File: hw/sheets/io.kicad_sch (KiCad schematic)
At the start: 23 parts, among them J2 TYPE-C-31-M-12, J3 TE_292303-7, J4 Hirose_DM3D-SF, J5 Wuerth_694106301002, J6 AudioJack4_Ground, J7 SFW15R-2STE1LF, J8 SFW15R-2STE1LF, J9 TYPE-C-31-M-12, Q1 AO3401A, Q2 AO3401A

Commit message: Add MSC1 breakout (J37), ground J35 spare pads, add audio amp/mic tap (J38)
Carve J35's last 6 pins into a new MSC1 header (J37: CLK/CMD/D0-D3_CD),
keeping J35 at a fixed 26-pin size in both schematic and PCB with the
now-orphaned pads tied to GND. Add a 3-pin tap (J38) off the audio jack
(HPOUTL/GND/MICLP) so an external amplifier or mic can be wired in
directly instead of needing a breakout cable off J6.
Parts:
- added J38: AMP_MIC_TAP, Connector_PinHeader_2.54mm:PinHeader_1x03_P2.54mm_Vertical, symbol Connector_Generic:Conn_01x03
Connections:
- net GND: now also J38.2 (Pin_2)
- net HPOUTL: now also J38.1 (Pin_1)
- net MICLP: now also J38.3 (Pin_3)
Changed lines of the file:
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@@
 		(property "Value" "GND" (at 60.96 241.3 270) (effects (font (size 1.27 1.27))))
+	)
+	(symbol (lib_id "Connector_Generic:Conn_01x03") (at 88.9 241.3 0) (unit 1)
+		(property "Reference" "J38" (at 93.98 238.76000000000002 0) (effects (font (size 1.27 1.27))))
+		(property "Value" "AMP_MIC_TAP" (at 93.98 243.84 0) (effects (font (size 1.27 1.27))))
+		(property "Footprint" "Connector_PinHeader_2.54mm:PinHeader_1x03_P2.54mm_Vertical" (at 88.9 241.3 0) (effects (font (size 1.27 1.27)) hide))
+	)
+	(symbol (lib_id "power:GND") (at 83.82 241.3 270) (unit 1)
+		(property "Reference" "#IGND020" (at 83.82 241.3 0) (effects (font (size 1.27 1.27)) hide))
+		(property "Value" "GND" (at 78.74 241.3 90) (effects (font (size 1.27 1.27))))
 	)
 	(symbol (lib_id "teacup-carrier:SFW15R-2STE1LF_C3167933") (at 190.5 50.8 0) (unit 1)
@@
 	)
 	(symbol (lib_id "power:GND") (at 185.42 45.72 270) (unit 1)
-		(property "Reference" "#IGND020" (at 185.42 45.72 0) (effects (font (size 1.27 1.27)) hide))
+		(property "Reference" "#IGND021" (at 185.42 45.72 0) (effects (font (size 1.27 1.27)) hide))
 		(property "Value" "GND" (at 180.33999999999997 45.72 90) (effects (font (size 1.27 1.27))))
 	)
 	(symbol (lib_id "power:GND") (at 185.42 53.34 270) (unit 1)
-		(property "Reference" "#IGND021" (at 185.42 53.34 0) (effects (font (size 1.27 1.27)) hide))
+		(property "Reference" "#IGND022" (at 185.42 53.34 0) (effects (font (size 1.27 1.27)) hide))
 		(property "Value" "GND" (at 180.33999999999997 53.34 90) (effects (font (size 1.27 1.27))))
 	)
 	(symbol (lib_id "power:GND") (at 185.42 60.96 270) (unit 1)
-		(property "Reference" "#IGND022" (at 185.42 60.96 0) (effects (font (size 1.27 1.27)) hide))
+		(property "Reference" "#IGND023" (at 185.42 60.96 0) (effects (font (size 1.27 1.27)) hide))
 		(property "Value" "GND" (at 180.33999999999997 60.96 90) (effects (font (size 1.27 1.27))))
 	)
 	(symbol (lib_id "power:GND") (at 185.42 68.58 270) (unit 1)
-		(property "Reference" "#IGND023" (at 185.42 68.58 0) (effects (font (size 1.27 1.27)) hide))
+		(property "Reference" "#IGND024" (at 185.42 68.58 0) (effects (font (size 1.27 1.27)) hide))
 		(property "Value" "GND" (at 180.33999999999997 68.58 90) (effects (font (size 1.27 1.27))))
 	)
@@
 	)
 	(symbol (lib_id "power:GND") (at 185.42 121.92 270) (unit 1)
-		(property "Reference" "#IGND024" (at 185.42 121.92 0) (effects (font (size 1.27 1.27)) hide))
+		(property "Reference" "#IGND025" (at 185.42 121.92 0) (effects (font (size 1.27 1.27)) hide))
 		(property "Value" "GND" (at 180.33999999999997 121.92 90) (effects (font (size 1.27 1.27))))
 	)
 	(symbol (lib_id "power:GND") (at 185.42 129.54 270) (unit 1)
-		(property "Reference" "#IGND025" (at 185.42 129.54 0) (effects (font (size 1.27 1.27)) hide))
+		(property "Reference" "#IGND026" (at 185.42 129.54 0) (effects (font (size 1.27 1.27)) hide))
 		(property "Value" "GND" (at 180.33999999999997 129.54 90) (effects (font (size 1.27 1.27))))
 	)
 	(symbol (lib_id "power:GND") (at 185.42 137.16 270) (unit 1)
-		(property "Reference" "#IGND026" (at 185.42 137.16 0) (effects (font (size 1.27 1.27)) hide))
+		(property "Reference" "#IGND027" (at 185.42 137.16 0) (effects (font (size 1.27 1.27)) hide))
 		(property "Value" "GND" (at 180.33999999999997 137.16 90) (effects (font (size 1.27 1.27))))
 	)
 	(symbol (lib_id "power:GND") (at 185.42 144.78 270) (unit 1)
-		(property "Reference" "#IGND027" (at 185.42 144.78 0) (effects (font (size 1.27 1.27)) hide))
+		(property "Reference" "#IGND028" (at 185.42 144.78 0) (effects (font (size 1.27 1.27)) hide))
 		(property "Value" "GND" (at 180.33999999999997 144.78 90) (effects (font (size 1.27 1.27))))
 	)
@@
 	(global_label "HPOUTL" (at 55.88 243.84 0) (effects (font (size 1.27 1.27)) (justify left)))
 	(global_label "MICLP" (at 55.88 238.76 0) (effects (font (size 1.27 1.27)) (justify left)))
+	(global_label "HPOUTL" (at 83.82 238.76 180) (effects (font (size 1.27 1.27)) (justify right)))
+	(global_label "MICLP" (at 83.82 243.84 180) (effects (font (size 1.27 1.27)) (justify right)))
 	(global_label "MIPI0_SCCB_SDA" (at 185.42 35.56 180) (effects (font (size 1.27 1.27)) (justify right)))
 	(global_label "MIPI0_SCCB_SCL" (at 185.42 38.1 180) (effects (font (size 1.27 1.27)) (justify right)))

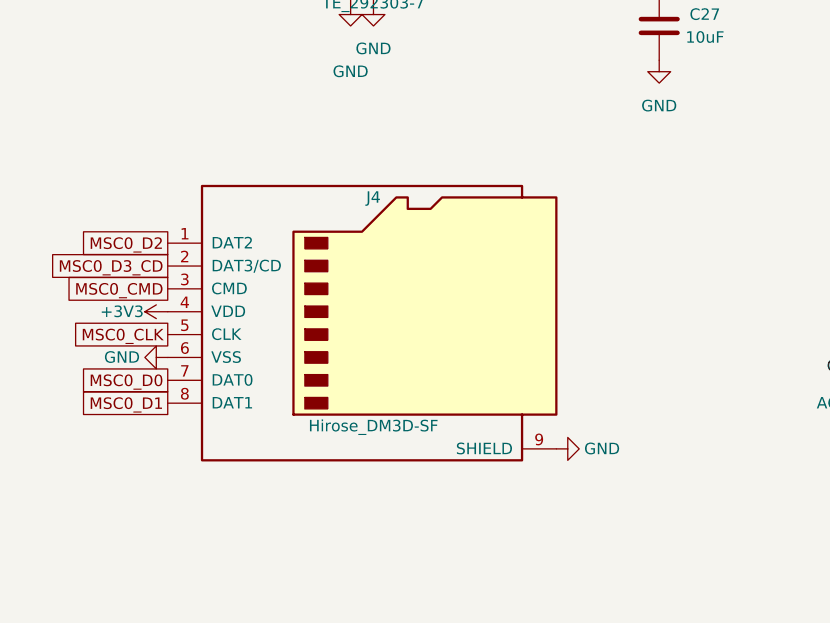
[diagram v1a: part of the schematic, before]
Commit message: Fix schematic<->PCB linking, reorder J1 pins by connected peer, add +3V3 plane, wire microSD card-detect
- schgen.py: deterministic per-symbol UUIDs (uuid5, keyed on ref designator)
  instead of random uuid4, so PCB footprints stay linked to their schematic
  symbol across regenerations; link all 133 real PCB footprints to their
  schematic symbol via path, fixing "Update PCB from Schematic" placing
  duplicates.
- J1 pin reorg: audio (HPOUTL/MICLP) moved from 170/171 to 6/7 (170/171 now
  GND); USBA_HOST_DP/DM moved from 40/41 to 20/21 (40/41 now GND); the 20
  pins connected directly to U8 (ESP32-S3) reordered so U8's ascending pin
  number maps to J1's descending pin number; +5V_MODEA (redundant -- a
  self-contained module already needs its own bare-bench power input)
  replaced with +5V_SW (the real arbitrated switched-5V rail) on pins 17/18.
- New +3V3 copper pour on In1.Cu, mirroring the existing GND pour; every
  +3V3 pad on the board (38, now 39 with R43) gets a stub trace + via down
  to it.
- microSD (J4): switched to the Micro_SD_Card_Det2 symbol so pin 10 (the
  footprint's real card-detect pad) has somewhere to attach; added R43
  (1M, matches TeaCup 3.3's R22) pulling MSC0_CD up to +3V3.
- fp-lib-table: replaced hardcoded /usr/share/kicad/footprints/... paths
  with ${KICAD10_FOOTPRINT_DIR}, fixing "footprint not found" errors for
  every component when Update PCB from Schematic runs outside this Linux
  environment.

Verified throughout via isolated ERC/DRC diffs against pre-change
baselines; each change confirmed to produce only its own intended delta.
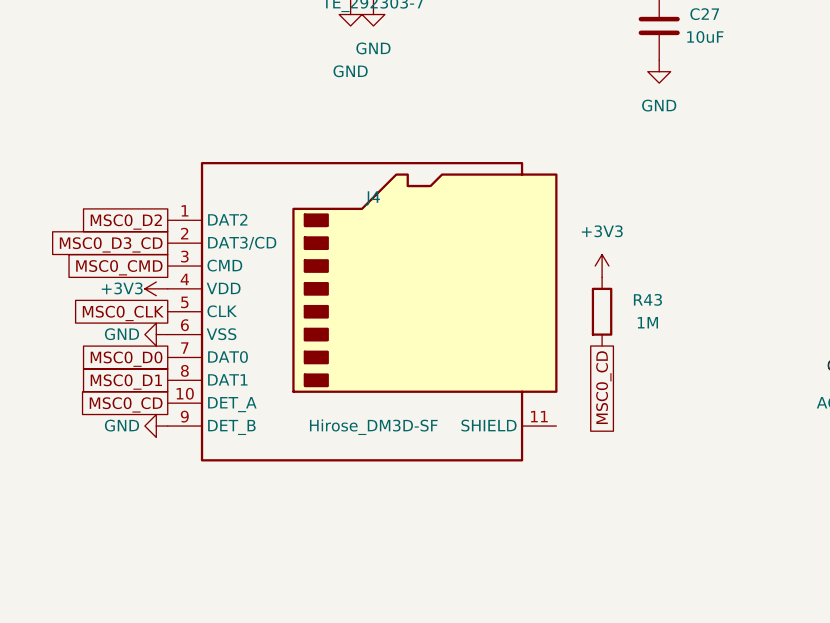
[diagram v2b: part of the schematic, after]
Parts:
- removed J4: Hirose_DM3D-SF, Connector_Card:microSD_HC_Hirose_DM3D-SF, symbol Connector:Micro_SD_Card
- added J4: Hirose_DM3D-SF, Connector_Card:microSD_HC_Hirose_DM3D-SF, symbol Connector:Micro_SD_Card_Det2
- added R43: 1M, Resistor_SMD:R_0402_1005Metric, symbol Device:R
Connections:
- net +3V3: now also J4.4 (VDD), R43.1
- net GND: now also J4.6 (VSS), J4.9 (DET_B)
- net MSC0_CLK: now also J4.5 (CLK)
- net MSC0_CMD: now also J4.3 (CMD)
- net MSC0_D0: now also J4.7 (DAT0)
- net MSC0_D1: now also J4.8 (DAT1)
- net MSC0_D2: now also J4.1 (DAT2)
- net MSC0_D3_CD: now also J4.2 (DAT3/CD)
- new net MSC0_CD: J4.10 (DET_A), R43.2
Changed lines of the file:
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@@
 		(property "Value" "GND" (at 48.26 132.07999999999998 0) (effects (font (size 1.27 1.27))))
 	)
-	(symbol (lib_id "Connector:Micro_SD_Card") (at 50.8 158.75 0) (unit 1)
+	(symbol (lib_id "Connector:Micro_SD_Card_Det2") (at 50.8 158.75 0) (unit 1)
 		(property "Reference" "J4" (at 50.8 146.05 0) (effects (font (size 1.27 1.27))))
 		(property "Value" "Hirose_DM3D-SF" (at 50.8 171.45 0) (effects (font (size 1.27 1.27))))
 		(property "Footprint" "Connector_Card:microSD_HC_Hirose_DM3D-SF" (at 50.8 158.75 0) (effects (font (size 1.27 1.27)) hide))
 	)
-	(symbol (lib_id "power:+3V3") (at 27.94 158.75 90) (unit 1)
-		(property "Reference" "#IPWR001" (at 27.94 158.75 0) (effects (font (size 1.27 1.27)) hide))
-		(property "Value" "+3V3" (at 22.86 158.75 270) (effects (font (size 1.27 1.27))))
+	(symbol (lib_id "power:+3V3") (at 27.94 156.21 90) (unit 1)
+		(property "Reference" "#IPWR001" (at 27.94 156.21 0) (effects (font (size 1.27 1.27)) hide))
+		(property "Value" "+3V3" (at 22.86 156.21 270) (effects (font (size 1.27 1.27))))
 	)
-	(symbol (lib_id "power:GND") (at 27.94 163.83 270) (unit 1)
-		(property "Reference" "#IGND015" (at 27.94 163.83 0) (effects (font (size 1.27 1.27)) hide))
-		(property "Value" "GND" (at 22.86 163.83 90) (effects (font (size 1.27 1.27))))
+	(symbol (lib_id "power:GND") (at 27.94 161.29 270) (unit 1)
+		(property "Reference" "#IGND015" (at 27.94 161.29 0) (effects (font (size 1.27 1.27)) hide))
+		(property "Value" "GND" (at 22.86 161.29 90) (effects (font (size 1.27 1.27))))
 	)
-	(symbol (lib_id "power:GND") (at 71.12 173.99 90) (unit 1)
-		(property "Reference" "#IGND016" (at 71.12 173.99 0) (effects (font (size 1.27 1.27)) hide))
-		(property "Value" "GND" (at 76.2 173.99 270) (effects (font (size 1.27 1.27))))
+	(symbol (lib_id "power:GND") (at 27.94 171.45 270) (unit 1)
+		(property "Reference" "#IGND016" (at 27.94 171.45 0) (effects (font (size 1.27 1.27)) hide))
+		(property "Value" "GND" (at 22.86 171.45 90) (effects (font (size 1.27 1.27))))
+	)
+	(symbol (lib_id "Device:R") (at 76.19999999999999 158.75 0) (unit 1)
+		(property "Reference" "R43" (at 81.27999999999999 157.48 0) (effects (font (size 1.27 1.27))))
+		(property "Value" "1M" (at 81.27999999999999 160.02 0) (effects (font (size 1.27 1.27))))
+		(property "Footprint" "Resistor_SMD:R_0402_1005Metric" (at 76.19999999999999 158.75 0) (effects (font (size 1.27 1.27)) hide))
+	)
+	(symbol (lib_id "power:+3V3") (at 76.2 154.94 0) (unit 1)
+		(property "Reference" "#IPWR002" (at 76.2 154.94 0) (effects (font (size 1.27 1.27)) hide))
+		(property "Value" "+3V3" (at 76.2 149.85999999999999 0) (effects (font (size 1.27 1.27))))
 	)
 	(symbol (lib_id "Connector:Barrel_Jack_Switch") (at 50.8 203.2 0) (unit 1)
@@
 	)
 	(symbol (lib_id "power:+3V3") (at 107.95 199.39 0) (unit 1)
-		(property "Reference" "#IPWR002" (at 107.95 199.39 0) (effects (font (size 1.27 1.27)) hide))
+		(property "Reference" "#IPWR003" (at 107.95 199.39 0) (effects (font (size 1.27 1.27)) hide))
 		(property "Value" "+3V3" (at 107.95 194.30999999999997 0) (effects (font (size 1.27 1.27))))
 	)
@@
 	)
 	(symbol (lib_id "power:+3V3") (at 185.42 33.02 90) (unit 1)
-		(property "Reference" "#IPWR003" (at 185.42 33.02 0) (effects (font (size 1.27 1.27)) hide))
+		(property "Reference" "#IPWR004" (at 185.42 33.02 0) (effects (font (size 1.27 1.27)) hide))
 		(property "Value" "+3V3" (at 180.33999999999997 33.02 270) (effects (font (size 1.27 1.27))))
 	)
 	(symbol (lib_id "power:+3V3") (at 185.42 40.64 90) (unit 1)
-		(property "Reference" "#IPWR004" (at 185.42 40.64 0) (effects (font (size 1.27 1.27)) hide))
+		(property "Reference" "#IPWR005" (at 185.42 40.64 0) (effects (font (size 1.27 1.27)) hide))
 		(property "Value" "+3V3" (at 180.33999999999997 40.64 270) (effects (font (size 1.27 1.27))))
 	)
@@
 	)
 	(symbol (lib_id "power:+3V3") (at 229.87 40.64 90) (unit 1)
-		(property "Reference" "#IPWR005" (at 229.87 40.64 0) (effects (font (size 1.27 1.27)) hide))
+		(property "Reference" "#IPWR006" (at 229.87 40.64 0) (effects (font (size 1.27 1.27)) hide))
 		(property "Value" "+3V3" (at 224.79 40.64 270) (effects (font (size 1.27 1.27))))
 	)
@@
 	)
 	(symbol (lib_id "power:+3V3") (at 185.42 109.22 90) (unit 1)
-		(property "Reference" "#IPWR006" (at 185.42 109.22 0) (effects (font (size 1.27 1.27)) hide))
+		(property "Reference" "#IPWR007" (at 185.42 109.22 0) (effects (font (size 1.27 1.27)) hide))
 		(property "Value" "+3V3" (at 180.33999999999997 109.22 270) (effects (font (size 1.27 1.27))))
 	)
 	(symbol (lib_id "power:+3V3") (at 185.42 116.84 90) (unit 1)
-		(property "Reference" "#IPWR007" (at 185.42 116.84 0) (effects (font (size 1.27 1.27)) hide))
+		(property "Reference" "#IPWR008" (at 185.42 116.84 0) (effects (font (size 1.27 1.27)) hide))
 		(property "Value" "+3V3" (at 180.33999999999997 116.84 270) (effects (font (size 1.27 1.27))))
 	)
@@
 	)
 	(symbol (lib_id "power:+3V3") (at 229.87 116.84 90) (unit 1)
-		(property "Reference" "#IPWR008" (at 229.87 116.84 0) (effects (font (size 1.27 1.27)) hide))
+		(property "Reference" "#IPWR009" (at 229.87 116.84 0) (effects (font (size 1.27 1.27)) hide))
 		(property "Value" "+3V3" (at 224.79 116.84 270) (effects (font (size 1.27 1.27))))
 	)
@@
 	(global_label "USBA_HOST_DM" (at 58.42 116.84 0) (effects (font (size 1.27 1.27)) (justify left)))
 	(global_label "USBA_HOST_DP" (at 58.42 114.3 0) (effects (font (size 1.27 1.27)) (justify left)))
-	(global_label "MSC0_D2" (at 27.94 151.13 180) (effects (font (size 1.27 1.27)) (justify right)))
-	(global_label "MSC0_D3_CD" (at 27.94 153.67 180) (effects (font (size 1.27 1.27)) (justify right)))
-	(global_label "MSC0_CMD" (at 27.94 156.21 180) (effects (font (size 1.27 1.27)) (justify right)))
-	(global_label "MSC0_CLK" (at 27.94 161.29 180) (effects (font (size 1.27 1.27)) (justify right)))
-	(global_label "MSC0_D0" (at 27.94 166.37 180) (effects (font (size 1.27 1.27)) (justify right)))
-	(global_label "MSC0_D1" (at 27.94 168.91 180) (effects (font (size 1.27 1.27)) (justify right)))
+	(global_label "MSC0_D2" (at 27.94 148.59 180) (effects (font (size 1.27 1.27)) (justify right)))
+	(global_label "MSC0_D3_CD" (at 27.94 151.13 180) (effects (font (size 1.27 1.27)) (justify right)))
+	(global_label "MSC0_CMD" (at 27.94 153.67 180) (effects (font (size 1.27 1.27)) (justify right)))
+	(global_label "MSC0_CLK" (at 27.94 158.75 180) (effects (font (size 1.27 1.27)) (justify right)))
+	(global_label "MSC0_D0" (at 27.94 163.83 180) (effects (font (size 1.27 1.27)) (justify right)))
+	(global_label "MSC0_D1" (at 27.94 166.37 180) (effects (font (size 1.27 1.27)) (justify right)))
+	(global_label "MSC0_CD" (at 27.94 168.91 180) (effects (font (size 1.27 1.27)) (justify right)))
+	(global_label "MSC0_CD" (at 76.2 162.56 270) (effects (font (size 1.27 1.27)) (justify right)))
 	(global_label "DCJACK_VBUS" (at 58.42 200.66 0) (effects (font (size 1.27 1.27)) (justify left)))
 	(global_label "DCJACK_PRESENT" (at 58.42 203.2 0) (effects (font (size 1.27 1.27)) (justify left)))
